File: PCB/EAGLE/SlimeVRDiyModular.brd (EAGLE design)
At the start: 39.4 x 39.5 mm, 50 parts, among them IC1 FT231XS-R, IC2 M3406-ADJ, IC6 DW01A, Q1 MMBT3904-TP, Q2 MMBT3904-TP, Q4 FS8205A, U3 TP4056, U4 ESP32-WROOM-32D, U6 SI2301BDS-T1-E3

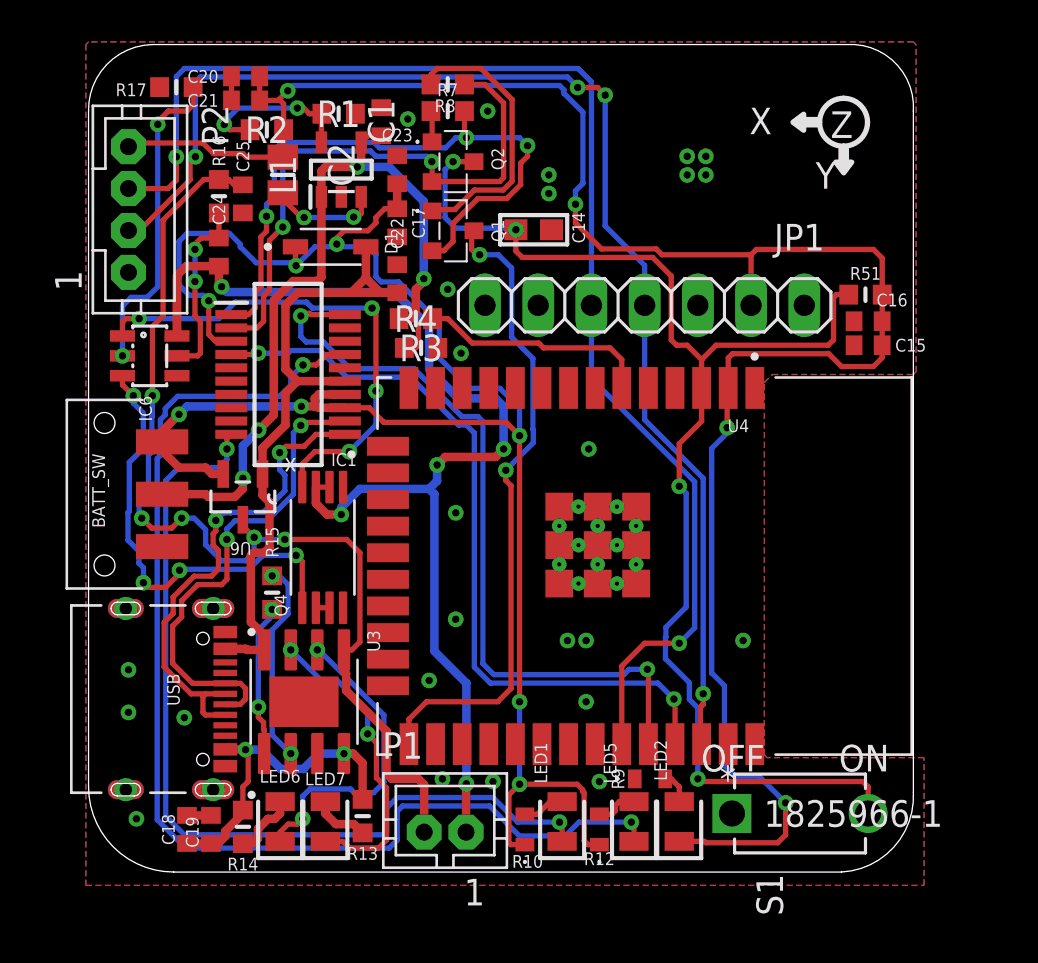
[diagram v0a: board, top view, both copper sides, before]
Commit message: FEAT: update 3D model, gerber and BOM
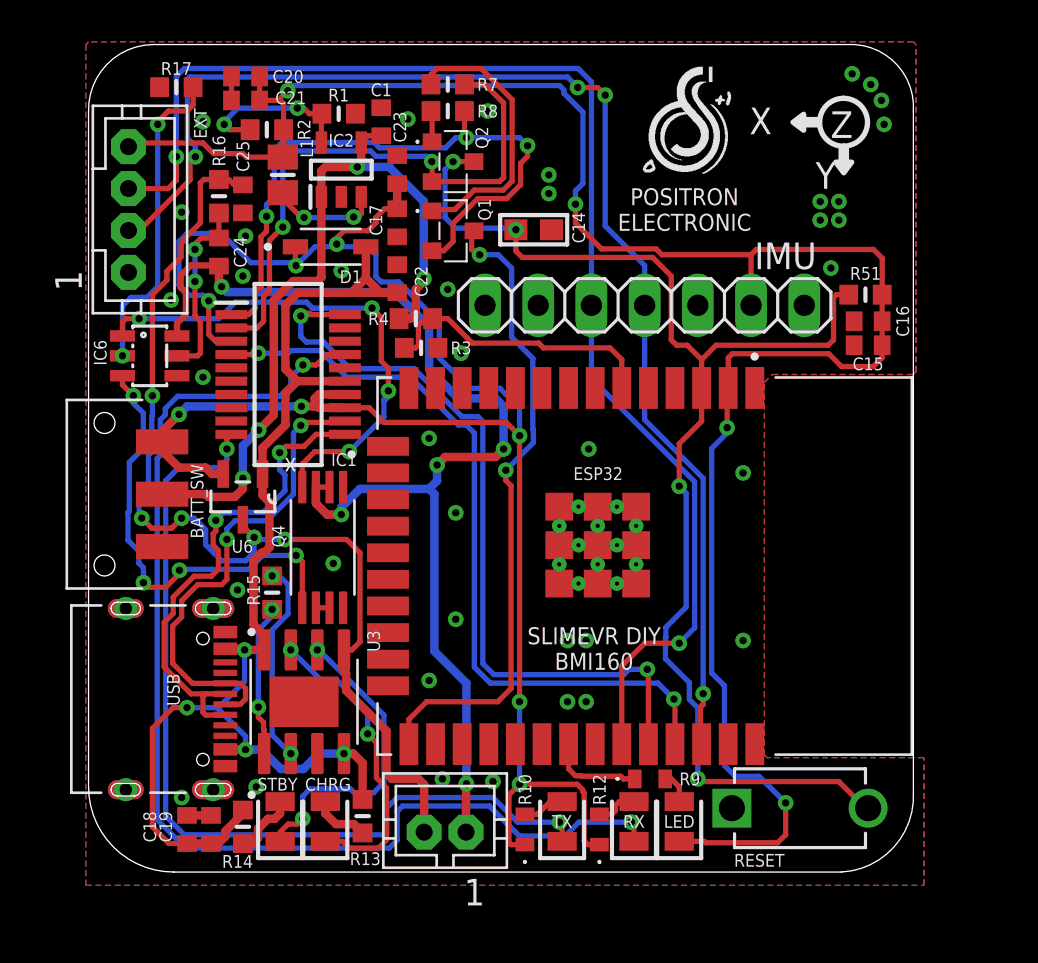
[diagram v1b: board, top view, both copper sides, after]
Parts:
- removed S1: 1825966-1, Switches:SWDIP2_256X170P100
- added RESET: 1825966-1, Switches:SWDIP2_256X170P100
- renumbered JP1 to IMU, LED1 to TX, LED2 to LED, LED5 to RX, LED6 to STBY, LED7 to CHRG, P2 to EXT, U4 to ESP32
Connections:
- removed net BUTTON2: ESP32.31
- removed net D2: R9.1
- new net LED: ESP32.31, R9.1
- net EN: now also RESET.2; no longer S1.2
- net GND: now also RESET.1; no longer S1.1
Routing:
- net VBUS: track 47.4 -> 60.4 mm, vias 2 -> 4
- net LED: track 0.00 -> 4.54 mm
- net VBAT-: track 57.7 -> 55.0 mm
- net EN: track 62.0 -> 61.1 mm
- net SCL: track 61.7 -> 62.3 mm
- net N$20: track 24.1 -> 24.7 mm
- net GND: vias 25 -> 39
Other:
- board text added: "POSITRON ELECTRONIC"
- board text added: "SLIMEVR DIY BMI160"
